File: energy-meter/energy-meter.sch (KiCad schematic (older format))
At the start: 33 parts, among them J1 Screw_Terminal_01x04, J2 Conn_01x03, J3 I2C OLED Display, etc., K1 G5RL-U1A-E, P1 PineNut, T1 AP-2500, T2 BV 202 0154, U1 L9110S, U9 GD32VF103

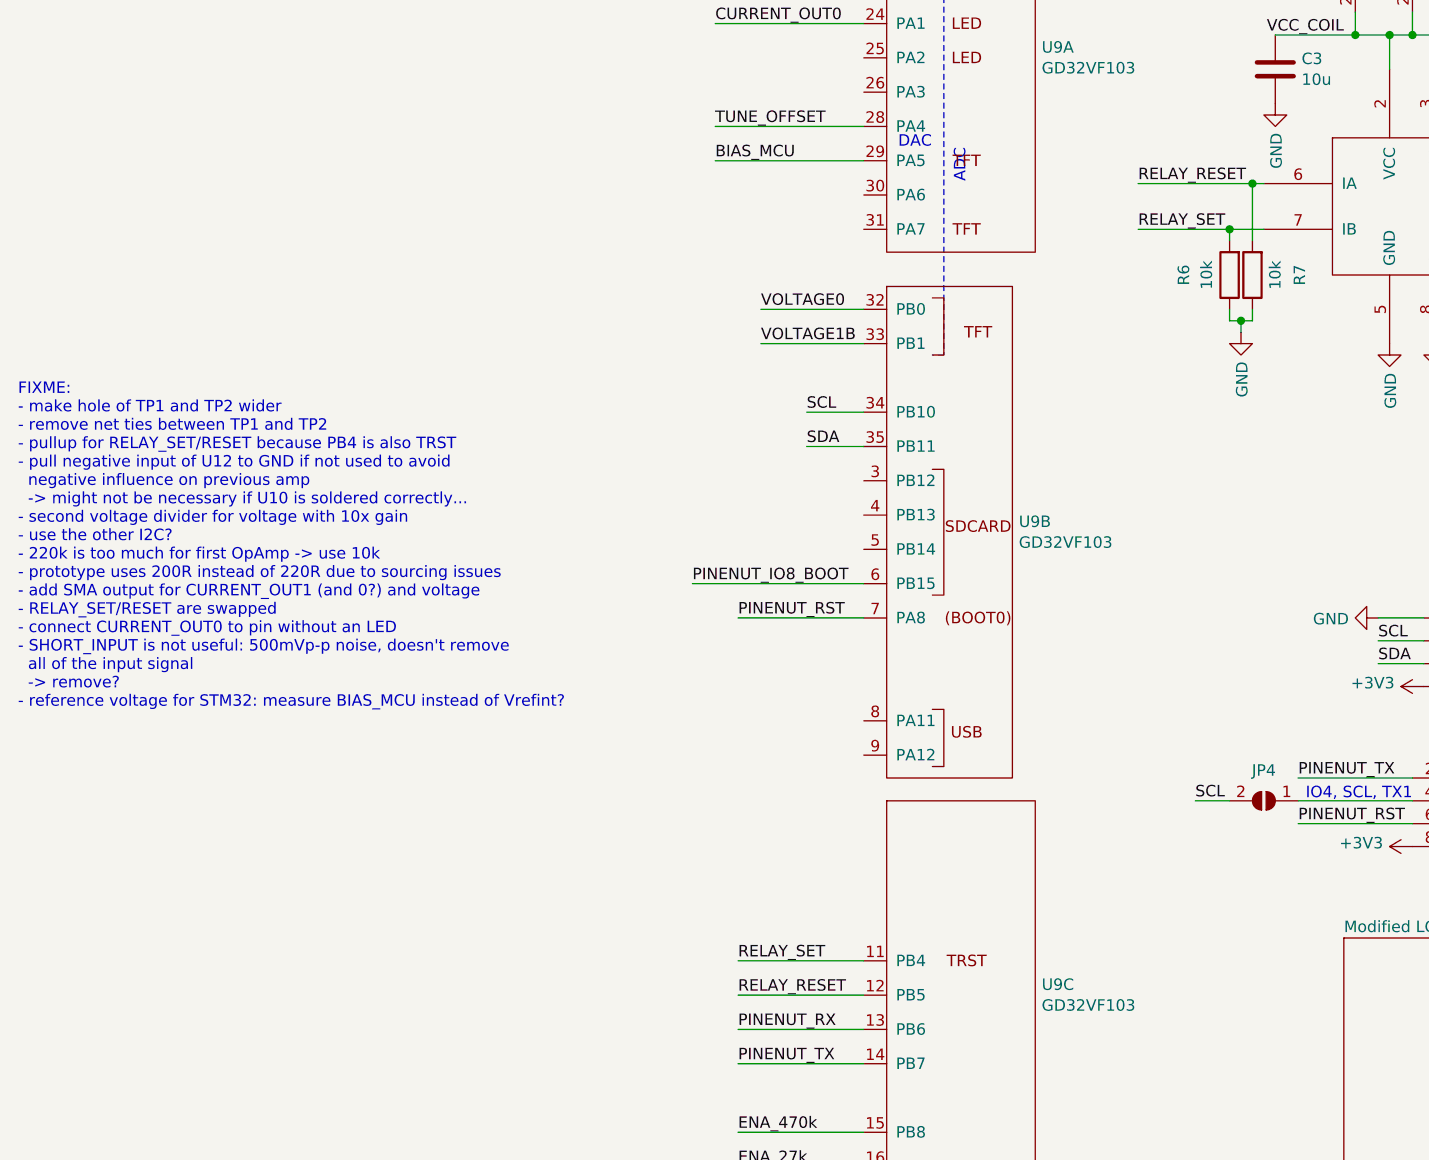
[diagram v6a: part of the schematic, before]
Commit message: increase size of test points for wire through current transformer, unswap RELAY_SET/RESET
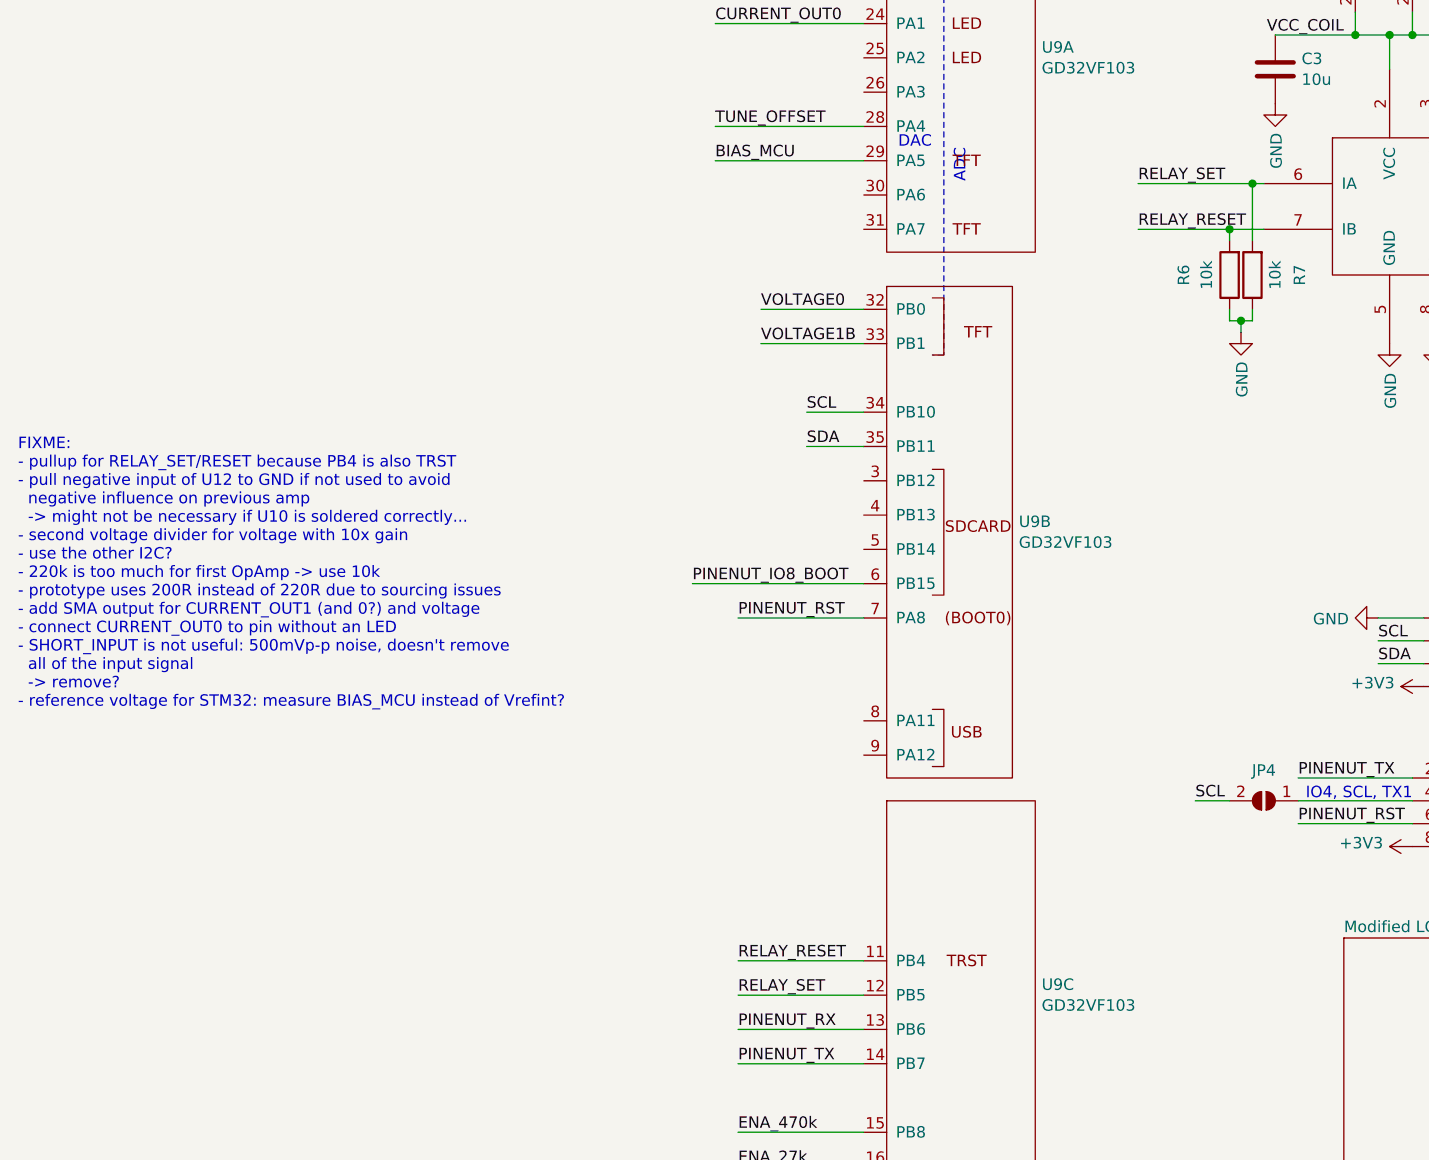
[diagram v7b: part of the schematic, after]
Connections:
- net RELAY_RESET: now also R6.2, U1.7 (IB), U9.11 (PB4); no longer R7.2, U1.6 (IA), U9.12 (PB5)
- net RELAY_SET: now also R7.2, U1.6 (IA), U9.12 (PB5); no longer R6.2, U1.7 (IB), U9.11 (PB4)
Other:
- note added: "FIXME:\n- pullup for RELAY_SET/RESET because PB4 is also TRST\n- pull negative input of U12 to GND if not used to avoid\n negative influence on previous amp\n -> might not be necessary if U10 is soldered correctly...\n- second voltage divider for voltage with 10x gain\n- use the other I2C?\n- 220k is too much for first OpAmp -> use 10k\n- prototype uses 200R instead of 220R due to sourcing issues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"
- note removed: "FIXME:\n- make hole of TP1 and TP2 wider\n- remove net ties between TP1 and TP2\n- pullup for RELAY_SET/RESET because PB4 is also TRST\n- pull negative input of U12 to GND if not used to avoid\n negative influence on previous amp\n -> might not be necessary if U10 is soldered correctly...\n- second voltage divider for voltage with 10x gain\n- use the other I2C?\n- 220k is too much for first OpAmp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"
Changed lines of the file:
@@
 Wire Wire Line
 	3150 2200 3000 2200
+Text Label 2600 2200 0    50   ~ 0
+RELAY_RESET
 Text Label 2600 2000 0    50   ~ 0
+RELAY_SET
+Text Label 850  5400 0    50   ~ 0
 RELAY_RESET
-Text Label 2600 2200 0    50   ~ 0
-RELAY_SET
 Text Label 850  5550 0    50   ~ 0
-RELAY_RESET
-Text Label 850  5400 0    50   ~ 0
 RELAY_SET
 Wire Wire Line
@@
 BIAS_MCU
 Text Notes -2300 4300 0    50   ~ 0
-FIXME:\n- make hole of TP1 and TP2 wider\n- remove net ties between TP1 and TP2\n- pullup for RELAY_SET/RESET because PB4 is also TRST\n- pull negative input of U12 to GND if not used to avoid\n  negative influence on previous amp\n  -> might not be necessary if U10 is soldered correctly...\n- second voltage divider for voltage with 10x gain\n- use the other I2C?\n- 220k is too much for first OpAmp -> use 10k\n- prototype uses 200R instead of 220R due to sourcing issues\n- add SMA output for CURRENT_OUT1 (and 0?) and voltage\n- RELAY_SET/RESET are swapped\n- connect CURRENT_OUT0 to pin without an LED\n- SHORT_INPUT is not useful: 500mVp-p noise, doesn't remove\n  all of the input signal\n  -> remove?\n- reference voltage for STM32: measure BIAS_MCU instead of Vrefint?
+FIXME:\n- pullup for RELAY_SET/RESET because PB4 is also TRST\n- pull negative input of U12 to GND if not used to avoid\n  negative influence on previous amp\n  -> might not be necessary if U10 is soldered correctly...\n- second voltage divider for voltage with 10x gain\n- use the other I2C?\n- 220k is too much for first OpAmp -> use 10k\n- prototype uses 200R instead of 220R due to sourcing issues\n- add SMA output for CURRENT_OUT1 (and 0?) and voltage\n- connect CURRENT_OUT0 to pin without an LED\n- SHORT_INPUT is not useful: 500mVp-p noise, doesn't remove\n  all of the input signal\n  -> remove?\n- reference voltage for STM32: measure BIAS_MCU instead of Vrefint?
 Text Notes 4650 2500 0    50   ~ 0
 datasheet: 120 mA\nmeasured, steady state: 107 mA

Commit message: handle most TODOs in schematic, PCB to be done
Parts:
- added C20: 10n, Capacitor_SMD:C_0603_1608Metric_Pad1.05x0.95mm_HandSolder, symbol Device:C
- added D7: ESD5Z5.0T1G, Diode_SMD:D_SOD-523, symbol Device:D_Zener
- added JP10, JP13, JP9: SolderJumper_2_Open, Jumper:SolderJumper-2_P1.3mm_Open_RoundedPad1.0x1.5mm, symbol Jumper:SolderJumper_2_Open
- added R8: 10k, 0.1%, Resistor_SMD:R_0603_1608Metric_Pad1.05x0.95mm_HandSolder, symbol Device:R
- R1: value 5k, 0.1% -> 10k, 0.1%
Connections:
- net +3V3: now also R6.1, R7.1
- net 6VAC: now also R8.1
- net CURRENT_OUT0: now also U9.23 (PA0); no longer U9.24 (PA1)
- net CURRENT_OUT1: now also U9.30 (PA6); no longer U9.23 (PA0)
- net GND: now also D7.2 (A); no longer R6.1, R7.1
- net PINENUT_RX: now also JP9.2 (B)
- net PINENUT_TX: now also JP10.2 (B)
- net SCL: now also JP9.1 (A)
- net SDA: now also JP10.1 (A)
- net VOLTAGE1: now also U9.31 (PA7), C20.1, D7.1 (K), R8.2
- net VOLTAGE1B: now also C20.2
- net at U9.5 (PB14): now also JP13.2 (B)
- new net PGOOD: JP13.1 (A)
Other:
- note added: "10.2V AC -> 14.4V p-p\n-> divide by 1/11\n(6V nominal but 10.2V for no load)"
- note added: "FIXME:\n- add SMA output for CURRENT_OUT1 (and 0?) and voltage\n- Falls ich rechts auf der Platine ein paar Pins vom GD32V wegoptimieren kann, könnte ich mehr Platz für das Kabel schaffen.\n -> Yes but needs lots of re-routing. TODO: make cutout bigger"
- note added: "don't divide\n-> more resolution but will clip"
- note removed: "6V AC -> 8.5V p-p\n-> divide by 1/6"
- note removed: "FIXME:\n- pullup for RELAY_SET/RESET because PB4 is also TRST\n- pull negative input of U12 to GND if not used to avoid\n negative influence on previous amp\n -> might not be necessary if U10 is soldered correctly...\n- second voltage divider for voltage with 10x gain\n- use the other I2C?\n- 220k is too much for first OpAmp -> use 10k\n- prototype uses 200R instead of 220R due to sourcing issues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"
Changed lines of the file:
@@
 	7550 2850 7750 2850
 Text Notes 8300 2700 0    50   ~ 0
-6V AC -> 8.5V p-p\n-> divide by 1/6
+10.2V AC -> 14.4V p-p\n-> divide by 1/11\n(6V nominal but 10.2V for no load)
 $Comp
 L Device:R R?
@@
 AR Path="/60A41CC6" Ref="R1"  Part="1"
 F 0 "R1" V 7693 2850 50  0000 C CNN
-F 1 "5k, 0.1%" V 7784 2850 50  0000 C CNN
+F 1 "10k, 0.1%" V 7784 2850 50  0000 C CNN
 F 2 "Resistor_SMD:R_0603_1608Metric_Pad1.05x0.95mm_HandSolder" V 7830 2850 50  0001 C CNN
 F 3 "~" H 7900 2850 50  0001 C CNN
@@
 Wire Wire Line
 	1400 2550 950  2550
-$Sheet
-S 3500 5300 1100 2250
-U 607B74C2
-F0 "Modified LCR Meter" 50
-F1 "lcr.sch" 50
-F2 "CURRENT1" I R 4600 5500 50
-F3 "CURRENT0" I R 4600 5400 50
-F4 "BIAS_MCU" I R 4600 5650 50
-F5 "TUNE_OFFSET0" I R 4600 5750 50
-F6 "CURRENT_OUT0" I R 4600 5850 50
-F7 "ENA_1000x" I R 4600 6300 50
-F8 "SHORT_CURRENT" I R 4600 6100 50
-F9 "CURRENT_OUT1" I R 4600 5950 50
-F10 "ENA_100x" I R 4600 6200 50
-$EndSheet
 $Comp
 L energy-meter:L9110S U1
@@
 	3000 2600 3000 2550
 Connection ~ 3050 2600
-$Comp
-L power:GND #PWR0140
-U 1 1 60E3FBEF
-P 3050 2650
-F 0 "#PWR0140" H 3050 2400 50  0001 C CNN
-F 1 "GND" V 3055 2522 50  0000 R CNN
-F 2 "" H 3050 2650 50  0001 C CNN
-F 3 "" H 3050 2650 50  0001 C CNN
-	1    3050 2650
-	1    0    0    -1
-$EndComp
 Wire Wire Line
 	7250 3550 7950 3550
@@
 Text Label 750  850  0    50   ~ 0
 ENA_1000x
-Text Label 750  1300 0    50   ~ 0
-CURRENT_OUT0
-Text Label 750  1150 0    50   ~ 0
-CURRENT_OUT1
 Text Notes 1550 1850 0    50   ~ 0
 DAC
@@
 Wire Wire Line
 	750  1150 1400 1150
-Wire Wire Line
-	1400 1300 750  1300
-Wire Wire Line
-	750  700  1400 700
 Text Label 750  1900 0    50   ~ 0
 BIAS_MCU
-Text Notes -2300 4300 0    50   ~ 0
-FIXME:\n- pullup for RELAY_SET/RESET because PB4 is also TRST\n- pull negative input of U12 to GND if not used to avoid\n  negative influence on previous amp\n  -> might not be necessary if U10 is soldered correctly...\n- second voltage divider for voltage with 10x gain\n- use the other I2C?\n- 220k is too much for first OpAmp -> use 10k\n- prototype uses 200R instead of 220R due to sourcing issues\n- add SMA output for CURRENT_OUT1 (and 0?) and voltage\n- connect CURRENT_OUT0 to pin without an LED\n- SHORT_INPUT is not useful: 500mVp-p noise, doesn't remove\n  all of the input signal\n  -> remove?\n- reference voltage for STM32: measure BIAS_MCU instead of Vrefint?
 Text Notes 4650 2500 0    50   ~ 0
 datasheet: 120 mA\nmeasured, steady state: 107 mA
@@
 Text Notes 5700 5800 0    118  ~ 0
 Mains voltage is dangerous!\nRead this first!
+$Comp
+L power:+3V3 #PWR?
+U 1 1 60CDFE99
+P 3050 2650
+AR Path="/607B74C2/60CDFE99" Ref="#PWR?"  Part="1"
+AR Path="/60CDFE99" Ref="#PWR0139"  Part="1"
+F 0 "#PWR0139" H 3050 2500 50  0001 C CNN
+F 1 "+3V3" V 3065 2778 50  0000 L CNN
+F 2 "" H 3050 2650 50  0001 C CNN
+F 3 "" H 3050 2650 50  0001 C CNN
+	1    3050 2650
+	-1   0    0    1
+$EndComp
+Text Label 9600 1750 0    50   ~ 0
+6VAC
+$Comp
+L Device:R R?
+U 1 1 60CE4DEC
+P 9600 1900
+AR Path="/602A3FC4/60CE4DEC" Ref="R?"  Part="1"
+AR Path="/60514CC5/60CE4DEC" Ref="R?"  Part="1"
+AR Path="/607B74C2/60CE4DEC" Ref="R?"  Part="1"
+AR Path="/60CE4DEC" Ref="R8"  Part="1"
+F 0 "R8" V 9393 1900 50  0000 C CNN
+F 1 "10k, 0.1%" V 9484 1900 50  0000 C CNN
+F 2 "Resistor_SMD:R_0603_1608Metric_Pad1.05x0.95mm_HandSolder" V 9530 1900 50  0001 C CNN
+F 3 "~" H 9600 1900 50  0001 C CNN
+	1    9600 1900
+	1    0    0    -1
+$EndComp
+Text Label 10050 2100 2    50   ~ 0
+VOLTAGE1
+Wire Wire Line
+	9600 2100 9600 2050
+$Comp
+L Device:C C?
+U 1 1 60CF2866
+P 9600 2300
+AR Path="/602A2F7F/60CF2866" Ref="C?"  Part="1"
+AR Path="/602A3FC4/60CF2866" Ref="C?"  Part="1"
+AR Path="/60514CC5/60CF2866" Ref="C?"  Part="1"
+AR Path="/607B74C2/60CF2866" Ref="C?"  Part="1"
+AR Path="/60CF2866" Ref="C20"  Part="1"
+F 0 "C20" H 9715 2346 50  0000 L CNN
+F 1 "10n" H 9715 2255 50  0000 L CNN
+F 2 "Capacitor_SMD:C_0603_1608Metric_Pad1.05x0.95mm_HandSolder" H 9638 2150 50  0001 C CNN
+F 3 "~" H 9600 2300 50  0001 C CNN
+	1    9600 2300
+	1    0    0    -1
+$EndComp
+Text Label 10100 2550 2    50   ~ 0
+VOLTAGE1B
+Wire Wire Line
+	10100 2550 9600 2550
+Wire Wire Line
+	9600 2450 9600 2550
+Text Notes 9800 1950 0    50   ~ 0
+don't divide\n-> more resolution but will clip
+$Comp
+L Device:D_Zener D7
+U 1 1 60D0D2E8
+P 10200 2300
+F 0 "D7" V 10154 2379 50  0000 L CNN
+F 1 "ESD5Z5.0T1G" V 10245 2379 50  0000 L CNN
+F 2 "Diode_SMD:D_SOD-523" H 10200 2300 50  0001 C CNN
+F 3 "https://www.onsemi.com/pub/Collateral/ESD5Z2.5T1-D.PDF" H 10200 2300 50  0001 C CNN
+	1    10200 2300
+	0    1    1    0
+$EndComp
+Wire Wire Line
+	9600 2150 9600 2100
+Connection ~ 9600 2100
+Wire Wire Line
+	9600 2100 10200 2100
+Wire Wire Line
+	10200 2150 10200 2100
+$Comp
+L power:GND #PWR0140
+U 1 1 60D21205
+P 10200 2450
+F 0 "#PWR0140" H 10200 2200 50  0001 C CNN
+F 1 "GND" V 10205 2322 50  0000 R CNN
+F 2 "" H 10200 2450 50  0001 C CNN
+F 3 "" H 10200 2450 50  0001 C CNN
+	1    10200 2450
+	1    0    0    -1
+$EndComp
+Text Label 950  2200 0    50   ~ 0
+VOLTAGE1
+Wire Wire Line
+	950  2200 1400 2200
+$Sheet
+S 3500 5300 1100 2250
+U 607B74C2
+F0 "Modified LCR Meter" 50
+F1 "lcr.sch" 50
+F2 "CURRENT1" I R 4600 5500 50
+F3 "CURRENT0" I R 4600 5400 50
+F4 "BIAS_MCU" I R 4600 5650 50
+F5 "TUNE_OFFSET0" I R 4600 5750 50
+F6 "CURRENT_OUT0" I R 4600 5850 50
+F7 "ENA_1000x" I R 4600 6300 50
+F8 "SHORT_CURRENT" I R 4600 6100 50
+F9 "CURRENT_OUT1" I R 4600 5950 50
+F10 "ENA_100x" I R 4600 6200 50
+F11 "PGOOD" I R 4600 6400 50
+$EndSheet
+Wire Wire Line
+	4600 6400 5250 6400
+Text Label 5250 6400 2    50   ~ 0
+PGOOD
+Text Label 650  3600 0    50   ~ 0
+PGOOD
+$Comp
+L Jumper:SolderJumper_2_Open JP13
+U 1 1 60D7134F
+P 1150 3600
+F 0 "JP13" H 1150 3467 50  0000 C CNN
+F 1 "SolderJumper_2_Open" H 1150 3714 50  0001 C CNN
+F 2 "Jumper:SolderJumper-2_P1.3mm_Open_RoundedPad1.0x1.5mm" H 1150 3600 50  0001 C CNN
+F 3 "~" H 1150 3600 50  0001 C CNN
+	1    1150 3600
+	1    0    0    1
+$EndComp
+Wire Wire Line
+	1400 3600 1300 3600
+Wire Wire Line
+	1000 3600 650  3600
+Text Label 550  5500 3    50   ~ 0
+SCL
+Text Label 550  6100 1    50   ~ 0
+SDA
+$Comp
+L Jumper:SolderJumper_2_Open JP9
+U 1 1 60D93356
+P 700 5700
+F 0 "JP9" H 700 5567 50  0000 C CNN
+F 1 "SolderJumper_2_Open" H 700 5814 50  0001 C CNN
+F 2 "Jumper:SolderJumper-2_P1.3mm_Open_RoundedPad1.0x1.5mm" H 700 5700 50  0001 C CNN
+F 3 "~" H 700 5700 50  0001 C CNN
+	1    700  5700
+	1    0    0    1
+$EndComp
+$Comp
+L Jumper:SolderJumper_2_Open JP10
+U 1 1 60D938A6
+P 700 5850
+F 0 "JP10" H 700 5950 50  0000 C CNN
+F 1 "SolderJumper_2_Open" H 700 5964 50  0001 C CNN
+F 2 "Jumper:SolderJumper-2_P1.3mm_Open_RoundedPad1.0x1.5mm" H 700 5850 50  0001 C CNN
+F 3 "~" H 700 5850 50  0001 C CNN
+	1    700  5850
+	1    0    0    1
+$EndComp
+Wire Wire Line
+	550  6100 550  5850
+Wire Wire Line
+	550  5500 550  5700
+Text Label 750  2050 0    50   ~ 0
+CURRENT_OUT1
+Text Label 750  1150 0    50   ~ 0
+CURRENT_OUT0
+Wire Wire Line
+	750  700  1400 700
+Text Notes -4700 4700 0    50   ~ 0
+FIXME:\n- add SMA output for CURRENT_OUT1 (and 0?) and voltage\n- Falls ich rechts auf der Platine ein paar Pins vom GD32V wegoptimieren kann, könnte ich mehr Platz für das Kabel schaffen.\n  -> Yes but needs lots of re-routing. TODO: make cutout bigger
+Wire Wire Line
+	750  2050 1400 2050
 $EndSCHEMATC
